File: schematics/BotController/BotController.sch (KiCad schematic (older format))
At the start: 29 parts, among them IC1 ATMEGA644A-P, P1 UM2102 - UART2USB, P10 Stepper Upperarm, P11 Stepper Shoulder, P2 Herkulex Servo, P3 Encoder Socket 0, P4 Encoder Socket, P5 Stepper 1 WristTurn, P6 POWER uC, P7 POWER_SERVO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

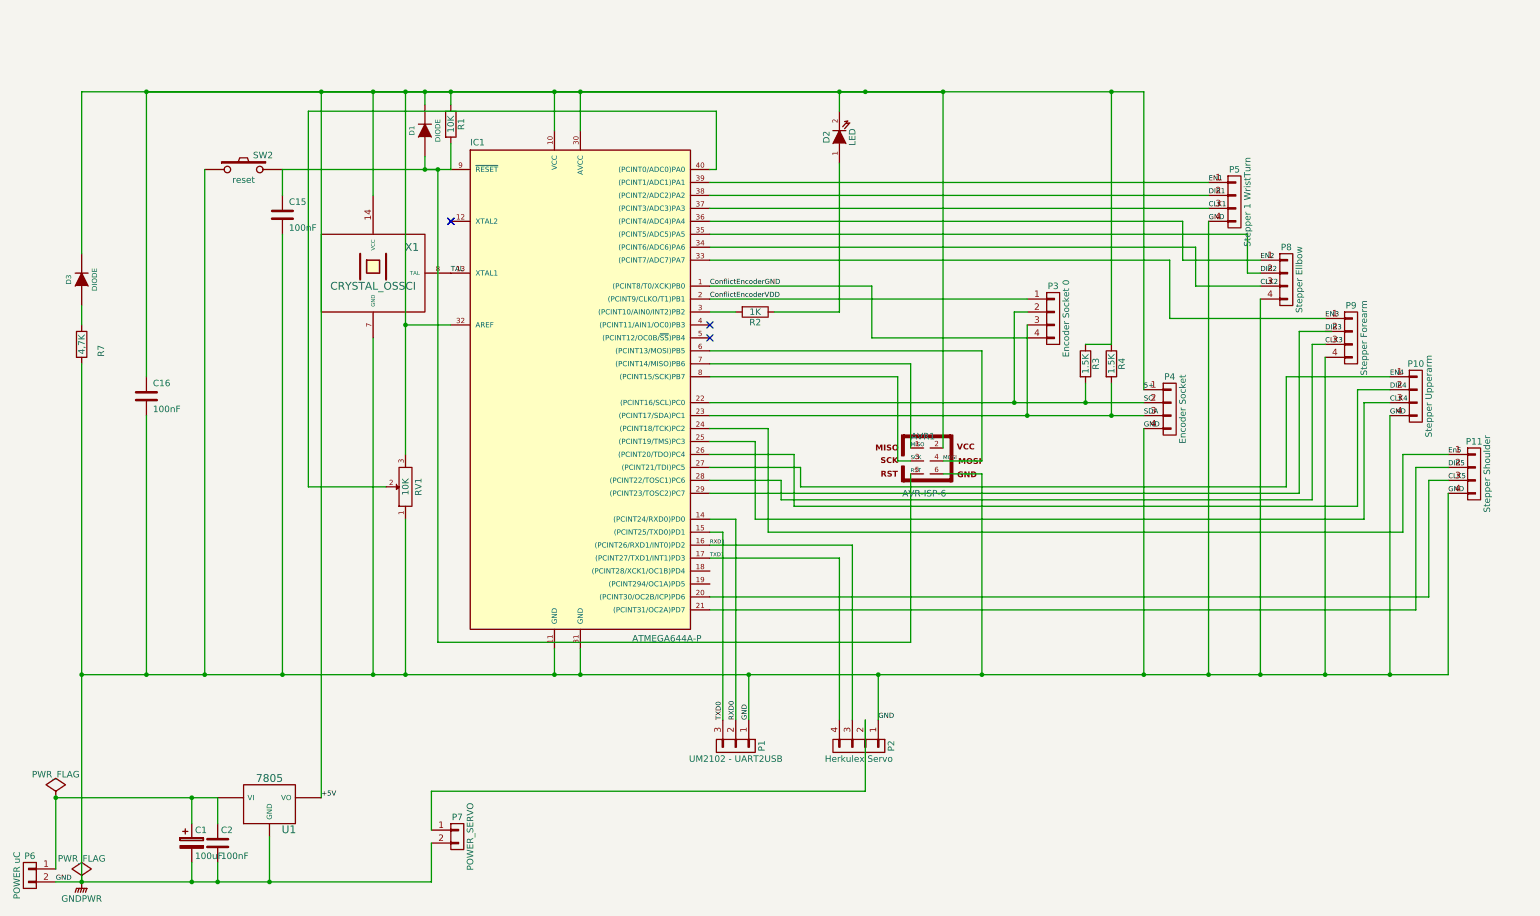
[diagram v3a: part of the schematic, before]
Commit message: PCB bekommt die letzten 4 PINs als enhancement Stecker Handgelenk vom Rest des entfernbaren Motordecksl bereinigt
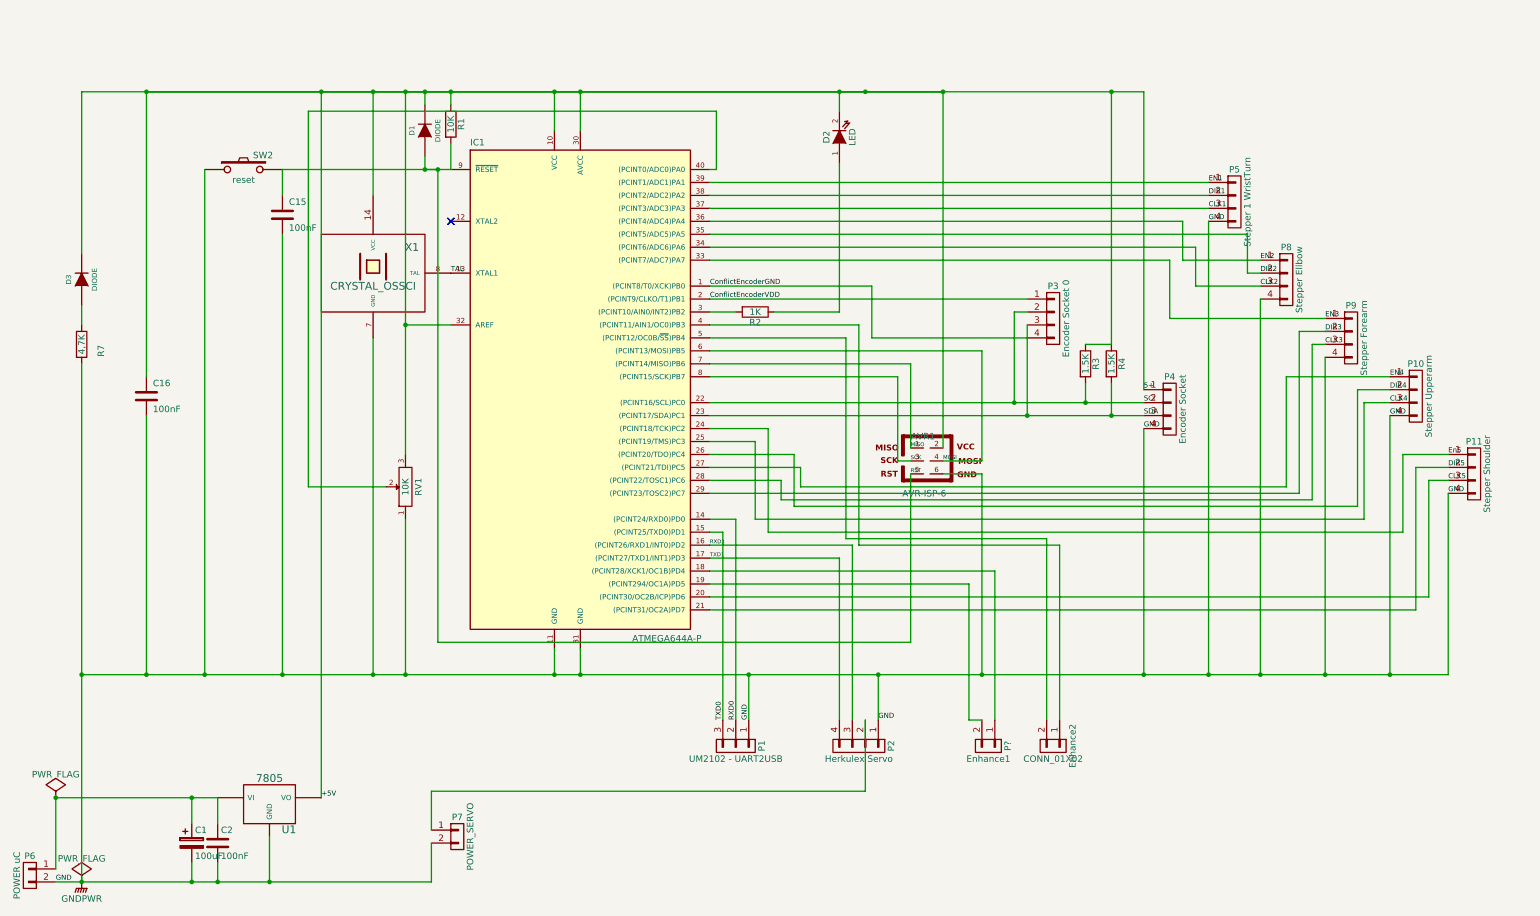
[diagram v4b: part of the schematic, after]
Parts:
- added Enhance2: CONN_01X02, symbol CONN_01X02
- added P?: Enhance1, symbol CONN_01X02
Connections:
- net at IC1.18 ((PCINT28/XCK1/OC1B)PD4): now also P?.1 (P1)
- net at IC1.19 ((PCINT294/OC1A)PD5): now also P?.2 (P2)
- net at IC1.4 ((PCINT11/AIN1/OC0)PB3): now also Enhance2.1 (P1)
- net at IC1.5 ((PCINT12/OC0B/~SS~)PB4): now also Enhance2.2 (P2)
- no-connect marks 6 -> 4
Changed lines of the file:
@@
 EESchema Schematic File Version 2
 LIBS:BotController-rescue
+LIBS:power
+LIBS:device
+LIBS:transistors
+LIBS:conn
+LIBS:linear
+LIBS:regul
+LIBS:74xx
+LIBS:cmos4000
+LIBS:adc-dac
+LIBS:memory
+LIBS:xilinx
+LIBS:microcontrollers
+LIBS:dsp
+LIBS:microchip
+LIBS:analog_switches
+LIBS:motorola
+LIBS:texas
+LIBS:intel
+LIBS:audio
+LIBS:interface
+LIBS:digital-audio
+LIBS:philips
+LIBS:display
+LIBS:cypress
+LIBS:siliconi
+LIBS:opto
+LIBS:atmel
+LIBS:contrib
+LIBS:valves
 LIBS:BotController-cache
 EELAYER 25 0
@@
 Text Label 6050 5300 0    30   ~ 0
 TXD1
-NoConn ~ 6050 3600
-NoConn ~ 6050 3500
 Text Label 7600 4650 0    30   ~ 0
 RST
@@
 	2750 2300 2750 2500
 Wire Wire Line
-	2750 2300 4050 2300
+	2750 2300 3850 2300
+Wire Wire Line
+	3850 2300 3950 2300
+Wire Wire Line
+	3950 2300 4050 2300
 Wire Wire Line
 	3950 5950 7600 5950
@@
 Connection ~ 3950 2300
 Wire Wire Line
-	1200 3800 1200 7800
+	1200 3800 1200 6200
+Wire Wire Line
+	1200 6200 1200 7800
 Wire Wire Line
 	29500 -12950 29500 -13950
@@
 Connection ~ 1700 6200
 Wire Wire Line
-	1200 1700 9400 1700
+	1200 1700 1700 1700
+Wire Wire Line
+	1700 1700 3050 1700
+Wire Wire Line
+	3050 1700 3450 1700
+Wire Wire Line
+	3450 1700 3700 1700
+Wire Wire Line
+	3700 1700 3850 1700
+Wire Wire Line
+	3850 1700 4050 1700
+Wire Wire Line
+	4050 1700 4850 1700
+Wire Wire Line
+	4850 1700 5050 1700
+Wire Wire Line
+	5050 1700 7050 1700
+Wire Wire Line
+	7050 1700 7250 1700
+Wire Wire Line
+	7250 1700 7850 1700
+Wire Wire Line
+	7850 1700 9150 1700
+Wire Wire Line
+	9150 1700 9400 1700
 Wire Wire Line
 	4050 1700 4050 1800
@@
 	3850 2300 3950 2300
 Wire Wire Line
-	1700 1700 7850 1700
+	1700 1700 3050 1700
+Wire Wire Line
+	3050 1700 3450 1700
+Wire Wire Line
+	3450 1700 3700 1700
+Wire Wire Line
+	3700 1700 3850 1700
+Wire Wire Line
+	3850 1700 4050 1700
+Wire Wire Line
+	4050 1700 4850 1700
+Wire Wire Line
+	4850 1700 5050 1700
+Wire Wire Line
+	5050 1700 7050 1700
+Wire Wire Line
+	7050 1700 7250 1700
+Wire Wire Line
+	7250 1700 7850 1700
 Wire Wire Line
 	8150 4550 7850 4550
@@
 	7500 3900 6050 3900
 Wire Wire Line
-	1200 6200 11750 6200
+	1200 6200 1700 6200
+Wire Wire Line
+	1700 6200 2150 6200
+Wire Wire Line
+	2150 6200 2750 6200
+Wire Wire Line
+	2750 6200 3450 6200
+Wire Wire Line
+	3450 6200 3700 6200
+Wire Wire Line
+	3700 6200 4850 6200
+Wire Wire Line
+	4850 6200 5050 6200
+Wire Wire Line
+	5050 6200 6350 6200
+Wire Wire Line
+	6350 6200 7350 6200
+Wire Wire Line
+	7350 6200 8150 6200
+Wire Wire Line
+	8150 6200 9400 6200
+Wire Wire Line
+	9400 6200 9900 6200
+Wire Wire Line
+	9900 6200 10300 6200
+Wire Wire Line
+	10300 6200 10800 6200
+Wire Wire Line
+	10800 6200 11300 6200
+Wire Wire Line
+	11300 6200 11750 6200
 Wire Wire Line
 	6350 6550 6350 6200
@@
 	4050 3500 3700 3500
 Wire Wire Line
-	3700 1700 3700 4500
+	3700 1700 3700 3500
+Wire Wire Line
+	3700 3500 3700 4500
 Wire Wire Line
 	3700 5000 3700 6200
@@
 	7050 5300 7050 6550
 Wire Wire Line
-	6050 4100 9400 4100
-Wire Wire Line
-	6050 4200 9400 4200
+	6050 4100 8400 4100
+Wire Wire Line
+	8400 4100 8950 4100
+Wire Wire Line
+	8950 4100 9400 4100
+Wire Wire Line
+	6050 4200 8500 4200
+Wire Wire Line
+	8500 4200 9150 4200
+Wire Wire Line
+	9150 4200 9400 4200
 Wire Wire Line
 	9400 6200 9400 4300
@@
 Connection ~ 1200 6200
 Wire Wire Line
-	1000 7800 3900 7800
+	1000 7800 1200 7800
+Wire Wire Line
+	1200 7800 2050 7800
+Wire Wire Line
+	2050 7800 2250 7800
+Wire Wire Line
+	2250 7800 2650 7800
+Wire Wire Line
+	2650 7800 3900 7800
 Wire Wire Line
 	2050 7800 2050 7650
@@
 	4850 6000 4850 6200
 Wire Wire Line
-	1000 7150 2250 7150
+	1000 7150 2050 7150
+Wire Wire Line
+	2050 7150 2250 7150
 Wire Wire Line
 	5050 6000 5050 6200
@@
 Wire Wire Line
 	11600 5600 6050 5600
+Wire Wire Line
+	6050 3500 7200 3500
+Wire Wire Line
+	7200 3500 7200 5200
+Wire Wire Line
+	7200 5200 8750 5200
+Wire Wire Line
+	8750 5200 8750 6550
+Wire Wire Line
+	6050 3600 7100 3600
+Wire Wire Line
+	7100 3600 7100 5150
+Wire Wire Line
+	7100 5150 8650 5150
+Wire Wire Line
+	8650 5150 8650 6550
+Wire Wire Line
+	6050 5400 8250 5400
+Wire Wire Line
+	8250 5400 8250 6550
+Wire Wire Line
+	6050 5500 8050 5500
+Wire Wire Line
+	8050 5500 8050 6550
+Wire Wire Line
+	8050 6550 8150 6550
+$Comp
+L CONN_01X02 Enhance2
+U 1 1 577920F3
+P 8700 6750
+F 0 "Enhance2" H 8700 6900 50  0000 C CNN
+F 1 "CONN_01X02" V 8800 6750 50  0000 C CNN
+F 2 "" H 8700 6750 50  0000 C CNN
+F 3 "" H 8700 6750 50  0000 C CNN
+	1    8700 6750
+	0    1    1    0
+$EndComp
+$Comp
+L CONN_01X02 P?
+U 1 1 577922A7
+P 8200 6750
+F 0 "P?" H 8200 6900 50  0000 C CNN
+F 1 "Enhance1" V 8300 6750 50  0000 C CNN
+F 2 "" H 8200 6750 50  0000 C CNN
+F 3 "" H 8200 6750 50  0000 C CNN
+	1    8200 6750
+	0    1    1    0
+$EndComp
 $EndSCHEMATC

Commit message: Ellenbogen gedruckt und Schaltung mit PowerSupply gemacht
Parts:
- removed P6: POWER uC, Connect:bornier2, symbol CONN_01X02
- removed P7: POWER_SERVO, Connect:bornier2, symbol CONN_01X02
- removed P?: Enhance1, symbol CONN_01X02
- added C11: 100uF, Capacitors_ThroughHole:C_Radial_D7.5_L11.2_P2.5, symbol CP
- added C12, C14: 100nF, Capacitors_ThroughHole:C_Disc_D3_P2.5, symbol C
- added C13: 1000uF, Capacitors_ThroughHole:C_Radial_D7.5_L11.2_P2.5, symbol CP
- added C7: 100uF, Capacitors_ThroughHole:C_Radial_D5_L6_P2.5, symbol CP
- added D10, D9: DIODE, Diodes_ThroughHole:Diode_DO-41_SOD81_Horizontal_RM10, symbol DIODE
- added D5: 1N5822, Diodes_ThroughHole:Diode_DO-41_SOD81_Horizontal_RM10, symbol DIODE
- added F1: FUSE, Pin_Headers:Pin_Header_Straight_1x02, symbol FUSE
- added P12: POWER_IN, Connect:bornier4, symbol CONN_01X04
- added P17: PowerEnableOut, Connectors_Molex:Molex_KK_6410-02, symbol CONN_01X02
- added P28: Power Stepper, Connect:bornier2, symbol CONN_01X02
- added P6: Power In uC Servo, Connectors_Molex:Molex_KK_6410-03, symbol CONN_01X03
- added P7: Power Out uC Servo, Connectors_Molex:Molex_KK_6410-03, symbol CONN_01X03
- added Q1, Q2: Q_NPN_BCE, TO_SOT_Packages_THT:TO-92_Inline_Wide, symbol Q_NPN_BCE
- added R10, R8: 1K, Discret:R4, symbol R
- added R5, R6: 120, Discret:R4, symbol R
- added REL1, REL2: Relay_1xON, BotController:RELAIS_HF115F, symbol Relay_1xON
- added U3: LM7809ACT, Power_Integrations:TO-220, symbol LM7809ACT
- P1: footprint Pin_Headers:Pin_Header_Straight_1x04 -> Pin_Headers:Pin_Header_Straight_1x03
- P13: renamed from Enhance2; value CONN_01X02 -> PowerEnableIn; footprint (none) -> Connectors_Molex:Molex_KK_6410-02
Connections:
- net +5V: now also C7.1
- net GNDPWR: now also C11.2, C12.2, C13.2, C14.2, C7.2, P12.4 (P4), P28.2 (P2), P6.1 (P1), P7.3 (P3), Q1.3 (E), Q2.3 (E), U3.2 (GND)
- net VDDServo: now reaches P2.2 (P2)
- net VDDServo: now also P6.3 (P3)
- net VDDuC: now reaches C1.1, C2.1, U1.VI
- net VDDuC: now also P6.2 (P2)
- new net: F1.2, REL2.3
- new net: C11.1, C12.1, D5.2 (K), R5.2, R6.2, U3.1 (IN)
- new net: D10.1 (A), Q2.2 (C), REL2.1
- new net: D10.2 (K), R5.1, REL2.2
- new net: P28.1 (P1), REL2.4
- new net: D9.1 (A), Q1.2 (C), REL1.1
- new net: D9.2 (K), R6.1, REL1.2
- new net: P17.1 (P1), R10.2
- new net: P17.2 (P2), R8.2
- new net: Q2.1 (B), R10.1
- new net: Q1.1 (B), R8.1
- new net 12V: D5.1 (A), P12.2 (P2)
- new net 24V: F1.1, P12.1 (P1)
- new net 5V: P12.3 (P3)
- new net VDD_Servo: P7.1 (P1), REL1.4
- new net VDD_uC: C13.1, C14.1, P7.2 (P2), REL1.3, U3.3 (OUT)
- no-connect marks 4 -> 12

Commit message: HostCommunication scheint zu gehen
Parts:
- removed D1, D10, D3, D9: DIODE, Diodes_ThroughHole:Diode_DO-41_SOD81_Horizontal_RM10, symbol DIODE
- removed D2: LED, LEDs:LED-3MM, symbol LED-RESCUE-BotController
- removed D5: 1N5822, Diodes_ThroughHole:Diode_DO-41_SOD81_Horizontal_RM10, symbol DIODE
- removed R7: 4,7K, Discret:R4, symbol R
- removed X1: CRYSTAL_OSSCI, BotController:OSC_DIP14, symbol CRYSTAL_OSSCI
- added C3: 100uF, Capacitors_ThroughHole:C_Radial_D5_L6_P2.5, symbol CP
- added C4, C5: 10uF, Capacitors_ThroughHole:C_Radial_D5_L6_P2.5, symbol CP
- added D1, D10: Diode, Diodes_ThroughHole:Diode_DO-35_SOD27_Horizontal_RM10, symbol D
- added D2: LED, LEDs:LED-3MM, symbol LED
- added D4: D, Diodes_ThroughHole:Diode_DO-35_SOD27_Horizontal_RM10, symbol D
- added D5: 1N5822, Diodes_ThroughHole:Diode_DO-35_SOD27_Horizontal_RM10, symbol D_Schottky
- added P14: ENHANCE, Connectors_Molex:Molex_KK_6410-02, symbol CONN_01X02
- added U2: LM7809ACT, Power_Integrations:TO-220, symbol LM7809ACT
- added X1: QUARZ_OSSCILATOR, BotController:OSC_DIP14, symbol QUARZ_OSSCILATOR
- F1: footprint Pin_Headers:Pin_Header_Straight_1x02 -> BotController:FUSE_HOLDER
- P1: footprint Pin_Headers:Pin_Header_Straight_1x03 -> Connectors_Molex:Molex_KK_6410-03
- P10, P11, P2, P3, P4, P5, P8, P9: footprint Pin_Headers:Pin_Header_Straight_1x04 -> Connectors_Molex:Molex_KK_6410-04
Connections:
- net labels added: LoggerTX, PowerOnServo, PowerOnStepper, PowerSupplyServo, PowerSupplyStepper
- wire segments 210 -> 284
- no-connect marks 12 -> 9
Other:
- moved on the sheet: P13, P17, R5, R6

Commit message: stepper geht jetzt wieder
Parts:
- P14: value ENHANCE -> Logger
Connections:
- wire segments 284 -> 215
- no-connect marks 9 -> 10
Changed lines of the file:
@@
 	2250 7150 2250 7350
 Wire Wire Line
-	1000 7150 2050 7150
-Wire Wire Line
-	2050 7150 2250 7150
+	1000 7150 2250 7150
 Wire Wire Line
 	2050 7800 2050 7650
@@
 Connection ~ 2050 7150
 Wire Wire Line
-	9900 2700 9900 6200
-Wire Wire Line
-	9900 6200 9900 6350
+	9900 2700 9900 6350
 Wire Wire Line
 	9400 1700 9400 4000
@@
 Connection ~ 3050 1700
 Wire Wire Line
-	3050 1700 3050 7150
-Wire Wire Line
-	3050 7150 3050 7300
+	3050 1700 3050 7300
 Connection ~ 2250 7800
 Connection ~ 2050 7800
 Wire Wire Line
-	950  7800 1200 7800
-Wire Wire Line
-	1200 7800 1750 7800
-Wire Wire Line
-	1750 7800 2050 7800
-Wire Wire Line
-	2050 7800 2250 7800
-Wire Wire Line
-	2250 7800 2650 7800
-Wire Wire Line
-	2650 7800 3050 7800
-Wire Wire Line
-	3050 7800 3900 7800
+	950  7800 3900 7800
 Wire Wire Line
 	7350 6200 7350 6550
@@
 	9400 6200 9400 4300
 Wire Wire Line
-	6050 4200 8500 4200
-Wire Wire Line
-	8500 4200 9150 4200
-Wire Wire Line
-	9150 4200 9400 4200
-Wire Wire Line
-	6050 4100 8400 4100
-Wire Wire Line
-	8400 4100 8950 4100
-Wire Wire Line
-	8950 4100 9400 4100
+	6050 4200 9400 4200
+Wire Wire Line
+	6050 4100 9400 4100
 Wire Wire Line
 	7050 5300 7050 6550
@@
 	3700 6200 3700 5000
 Wire Wire Line
-	3700 1700 3700 3500
-Wire Wire Line
-	3700 3500 3700 4500
+	3700 1700 3700 4500
 Wire Wire Line
 	4050 3500 3700 3500
@@
 	6350 6200 6350 6550
 Wire Wire Line
-	1200 6200 1700 6200
-Wire Wire Line
-	1700 6200 2150 6200
-Wire Wire Line
-	2150 6200 2750 6200
-Wire Wire Line
-	2750 6200 3450 6200
-Wire Wire Line
-	3450 6200 3700 6200
-Wire Wire Line
-	3700 6200 4850 6200
-Wire Wire Line
-	4850 6200 5050 6200
-Wire Wire Line
-	5050 6200 6350 6200
-Wire Wire Line
-	6350 6200 7350 6200
-Wire Wire Line
-	7350 6200 8150 6200
-Wire Wire Line
-	8150 6200 9400 6200
-Wire Wire Line
-	9400 6200 9900 6200
-Wire Wire Line
-	9900 6200 10300 6200
-Wire Wire Line
-	10300 6200 10800 6200
-Wire Wire Line
-	10800 6200 11300 6200
-Wire Wire Line
-	11300 6200 11750 6200
+	1200 6200 11750 6200
 Wire Wire Line
 	7500 3900 6050 3900
@@
 	8150 4550 7850 4550
 Wire Wire Line
-	1200 1700 1700 1700
-Wire Wire Line
-	1700 1700 3050 1700
-Wire Wire Line
-	3050 1700 3450 1700
-Wire Wire Line
-	3450 1700 3700 1700
-Wire Wire Line
-	3700 1700 3850 1700
-Wire Wire Line
-	3850 1700 4050 1700
-Wire Wire Line
-	4050 1700 4850 1700
-Wire Wire Line
-	4850 1700 5050 1700
-Wire Wire Line
-	5050 1700 7050 1700
-Wire Wire Line
-	7050 1700 7850 1700
-Wire Wire Line
-	7850 1700 9150 1700
-Wire Wire Line
-	9150 1700 9400 1700
-Wire Wire Line
-	2750 2300 3850 2300
-Wire Wire Line
-	3850 2300 3950 2300
-Wire Wire Line
-	3950 2300 4050 2300
+	1200 1700 9400 1700
+Wire Wire Line
+	2750 2300 4050 2300
 Connection ~ 3850 1700
 Connection ~ 3850 2300
@@
 	4050 1700 4050 1800
 Wire Wire Line
-	1700 1700 3050 1700
-Wire Wire Line
-	3050 1700 3450 1700
-Wire Wire Line
-	3450 1700 3700 1700
-Wire Wire Line
-	3700 1700 3850 1700
-Wire Wire Line
-	3850 1700 4050 1700
-Wire Wire Line
-	4050 1700 4850 1700
-Wire Wire Line
-	4850 1700 5050 1700
-Wire Wire Line
-	5050 1700 7050 1700
+	1700 1700 7050 1700
 Connection ~ 1700 6200
 Wire Wire Line
-	1700 4200 1700 6200
-Wire Wire Line
-	1700 6200 1700 7800
+	1700 4200 1700 7800
 Wire Wire Line
 	8150 3700 8150 4550
@@
 	950  8600 1150 8600
 Wire Wire Line
-	1650 8400 7550 8400
-Wire Wire Line
-	7550 8400 10050 8400
+	1650 8400 10050 8400
 Wire Wire Line
 	10700 10800 10700 10500
@@
 Connection ~ 6900 10800
 Wire Wire Line
-	6900 9950 7200 9950
-Wire Wire Line
-	7200 9950 7450 9950
+	6900 9950 7450 9950
 Wire Wire Line
 	7200 9950 7200 10250
@@
 	7650 10600 7650 10350
 Wire Wire Line
-	6000 10200 7650 10200
-Wire Wire Line
-	7650 10200 8200 10200
+	6000 10200 8200 10200
 Wire Wire Line
 	7650 10250 7650 10200
@@
 Connection ~ 10700 10800
 Wire Wire Line
-	4750 9950 5050 9950
-Wire Wire Line
-	5050 9950 6100 9950
+	4750 9950 6100 9950
 Wire Wire Line
 	2000 9550 4750 9550
 Wire Wire Line
-	4750 8950 4750 9550
-Wire Wire Line
-	4750 9550 4750 9950
-Wire Wire Line
-	4750 9950 4750 10300
+	4750 8950 4750 10300
 Connection ~ 4750 9950
 Connection ~ 4750 9550
@@
 	4750 8950 5700 8950
 Wire Wire Line
-	5700 8700 5700 8950
-Wire Wire Line
-	5700 8950 5700 10200
-Wire Wire Line
-	5700 10200 5700 10450
+	5700 8700 5700 10450
 Wire Wire Line
 	950  8600 950  9450
@@
 	10700 9950 10700 10300
 Wire Wire Line
-	950  10800 4750 10800
-Wire Wire Line
-	4750 10800 5050 10800
-Wire Wire Line
-	5050 10800 6500 10800
-Wire Wire Line
-	6500 10800 6850 10800
-Wire Wire Line
-	6850 10800 6900 10800
-Wire Wire Line
-	6900 10800 7200 10800
-Wire Wire Line
-	7200 10800 9450 10800
-Wire Wire Line
-	9450 10800 10000 10800
-Wire Wire Line
-	10000 10800 10700 10800
-Wire Wire Line
-	10700 10800 11050 10800
+	950  10800 11050 10800
 Text Label 10700 10400 0    39   ~ 0
 VDD_uC
@@
 $EndComp
 Wire Wire Line
-	4750 9400 4750 9550
-Wire Wire Line
-	4750 9550 4750 9950
+	4750 9400 4750 9950
 Wire Wire Line
 	4750 9400 9050 9400
@@
 Connection ~ 9450 10800
 Wire Wire Line
-	9850 9400 10000 9400
-Wire Wire Line
-	10000 9400 10500 9400
+	9850 9400 10500 9400
 Wire Wire Line
 	10000 9400 10000 9500
@@
 P 6750 5450
 F 0 "P14" H 6750 5600 50  0000 C CNN
-F 1 "ENHANCE" V 6850 5450 50  0000 C CNN
+F 1 "Logger" V 6850 5450 50  0000 C CNN
 F 2 "Connectors_Molex:Molex_KK_6410-02" H 6750 5450 50  0001 C CNN
 F 3 "" H 6750 5450 50  0000 C CNN
@@
 Wire Wire Line
 	6050 5400 6550 5400
-Wire Wire Line
-	6050 5500 6550 5500
 Wire Wire Line
 	1700 7800 1750 7800
@@
 Text Label 6550 5400 2    39   ~ 0
 LoggerTX
+NoConn ~ 6050 5500
+Wire Wire Line
+	6550 5500 6550 6200
+Connection ~ 6550 6200
+Text Label 6550 5500 1    39   ~ 0
+GND
 $EndSCHEMATC

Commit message: no message
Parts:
- C3: value 100uF -> 220uF
- R3: footprint Discret:R4 -> BotController:R4(8)
- R4: footprint Discret:R5 -> BotController:R4(7)
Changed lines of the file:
@@
 F 0 "R4" V 9230 3800 50  0000 C CNN
 F 1 "1.5K" V 9150 3800 50  0000 C CNN
-F 2 "Discret:R5" V 9080 3800 30  0001 C CNN
+F 2 "BotController:R4(7)" V 9080 3800 30  0001 C CNN
 F 3 "" H 9150 3800 30  0000 C CNN
 	1    9150 3800
@@
 F 0 "R3" V 9030 3800 50  0000 C CNN
 F 1 "1.5K" V 8950 3800 50  0000 C CNN
-F 2 "Discret:R4" V 8880 3800 30  0001 C CNN
+F 2 "BotController:R4(8)" V 8880 3800 30  0001 C CNN
 F 3 "" H 8950 3800 30  0000 C CNN
 	1    8950 3800
@@
 P 10000 9650
 F 0 "C3" H 10025 9750 50  0000 L CNN
-F 1 "100uF" H 10025 9550 50  0000 L CNN
+F 1 "220uF" H 10025 9550 50  0000 L CNN
 F 2 "Capacitors_ThroughHole:C_Radial_D5_L6_P2.5" H 10038 9500 50  0001 C CNN
 F 3 "" H 10000 9650 50  0000 C CNN
